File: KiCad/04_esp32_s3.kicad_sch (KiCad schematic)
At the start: 32 parts, among them IC401 ESP32-S3-WROOM-1-N16R8, J401 Conn_01x04_Pin, J402 Conn_01x04_Pin, J403 Conn_01x04_Pin, J404 TF-01A, J405 Conn_01x08_Pin, Q401 SS8050, Q402 SS8050

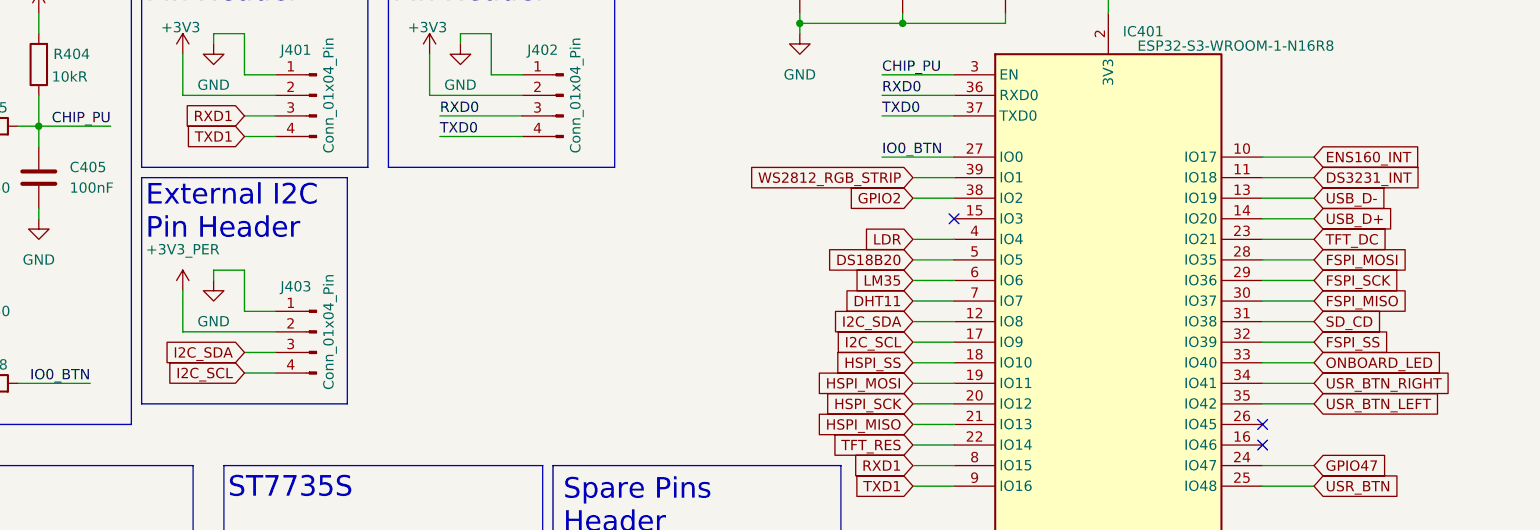
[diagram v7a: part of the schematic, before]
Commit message: Simple signal routing
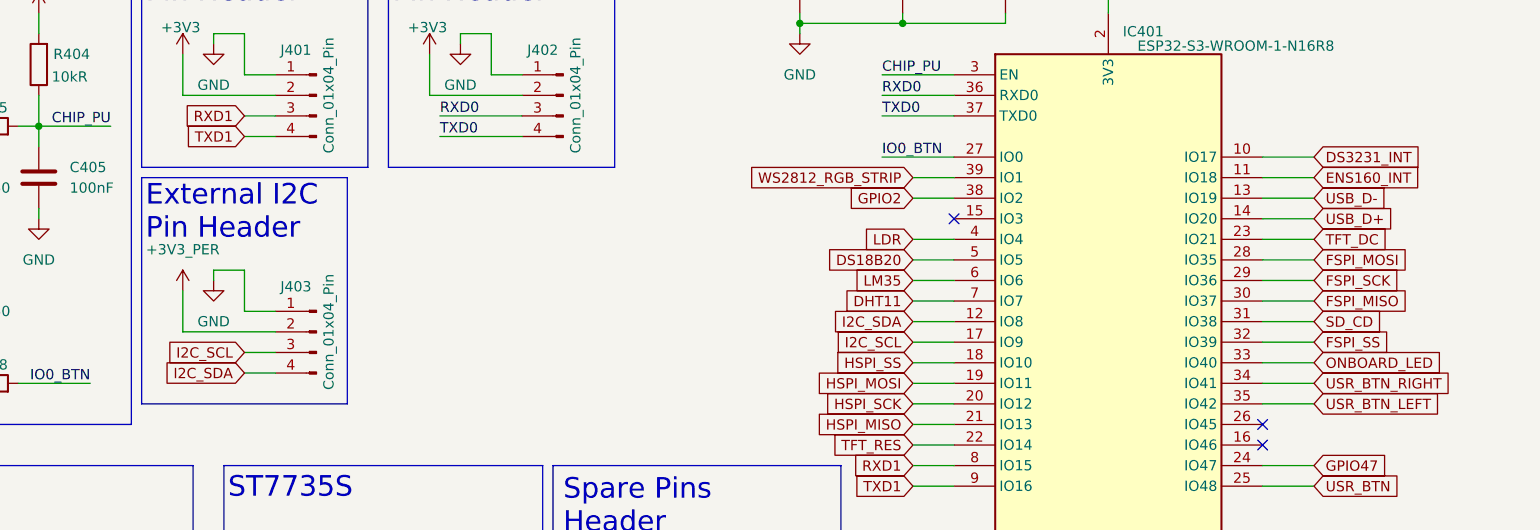
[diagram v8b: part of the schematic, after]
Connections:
- net DS3231_INT: now also IC401.10 (IO17); no longer IC401.11 (IO18)
- net ENS160_INT: now also IC401.11 (IO18); no longer IC401.10 (IO17)
- net I2C_SCL: now also J403.3 (Pin_3); no longer J403.4 (Pin_4)
- net I2C_SDA: now also J403.4 (Pin_4); no longer J403.3 (Pin_3)
